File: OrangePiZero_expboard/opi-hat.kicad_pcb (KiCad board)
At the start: 2 copper layers, 48 x 46 mm, 36 parts, among them J1 Hydreon, J2 I2C, J3 SPI, J4 12Vin, J5 USB_C_Receptacle_USB2.0, J6 USB_B, J7 5Vout, U1 PC817, U2 LM2576-5.0, U3 LM1117-3.3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

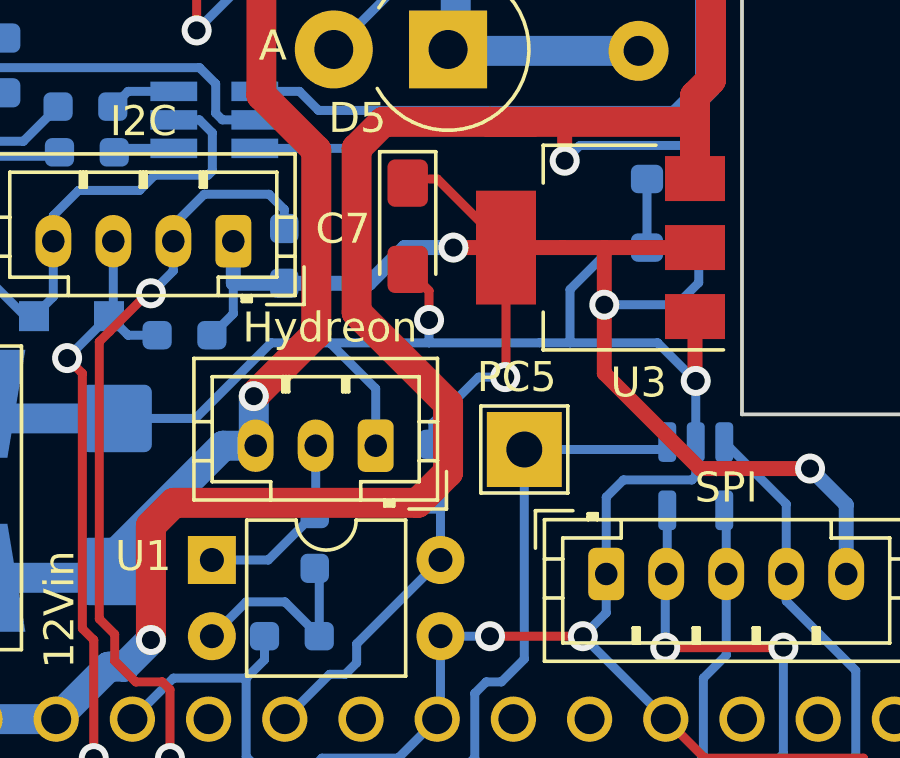
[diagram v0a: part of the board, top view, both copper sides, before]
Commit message: fixed boards on new kicad
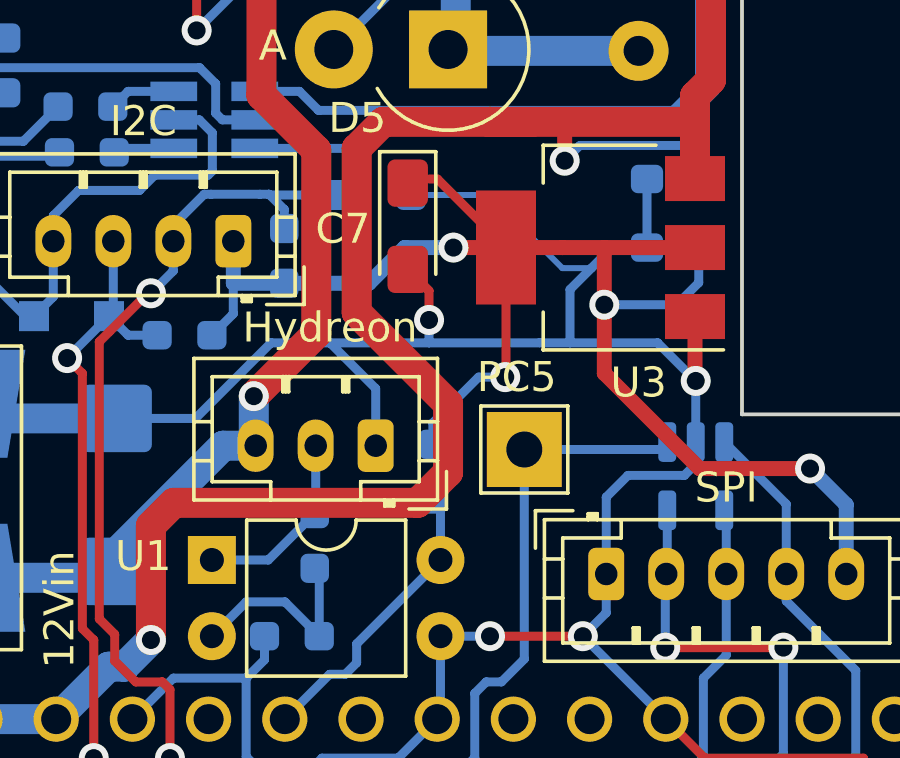
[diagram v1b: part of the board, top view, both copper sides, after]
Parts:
- added D2: CESD3V3, Diode_SMD:D_SOD-323_HandSoldering, B.Cu at (103.5, 76.2)
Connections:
- X1 pad 1: unconnected-(X1-Pad1) -> unconnected-(X1-3V3-Pad1)_0
- X1 pad 17: unconnected-(X1-Pad1) -> unconnected-(X1-3V3-Pad1)
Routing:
- net GND: track 273.3 -> 280.1 mm
- net /SCK: track 27.1 -> 29.4 mm
